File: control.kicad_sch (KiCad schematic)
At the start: 52 parts, among them J101 Cortex_Debug, J102 JAE_DX07S016JA3, J501 WAGO-2065, J502 WAGO-2065, SW101 SW_Push, SW102 SW_Push, U101 ATSAMD51G, U103 TPS78433QWDRBRQ1, Y101 32k768

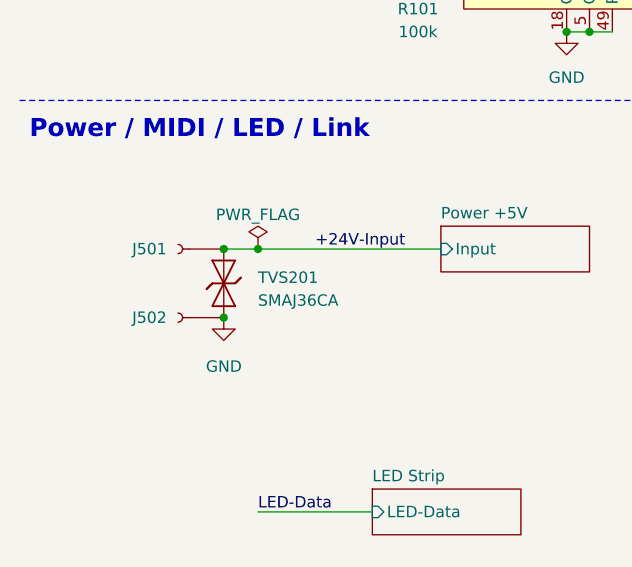
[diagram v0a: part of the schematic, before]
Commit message: Update to Kicad 8
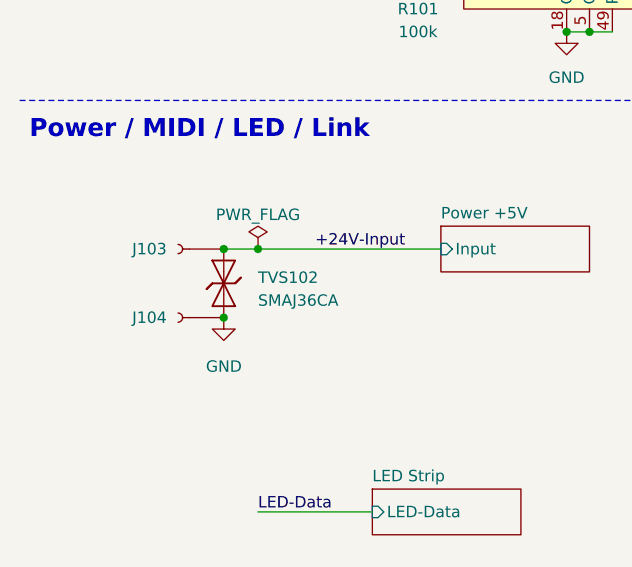
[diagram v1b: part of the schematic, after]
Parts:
- renumbered J501 to J103, J502 to J104, TVS201 to TVS102

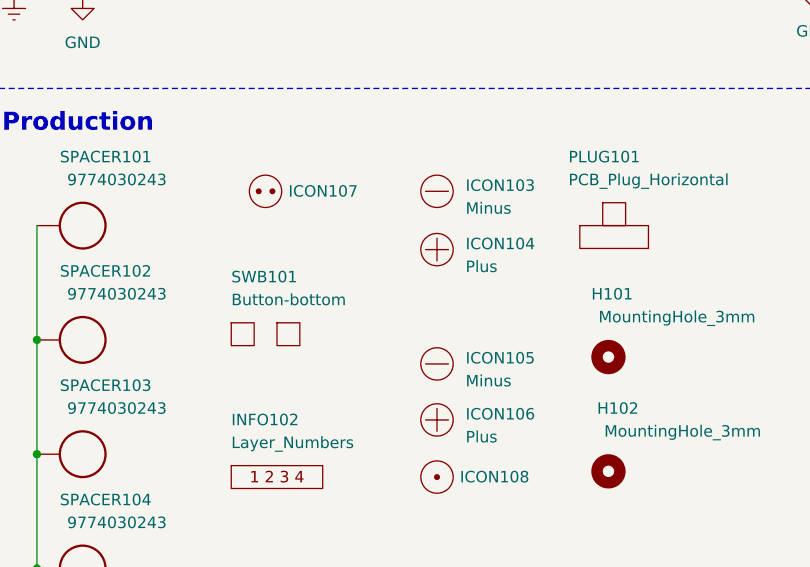
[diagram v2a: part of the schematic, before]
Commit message: Replace icons
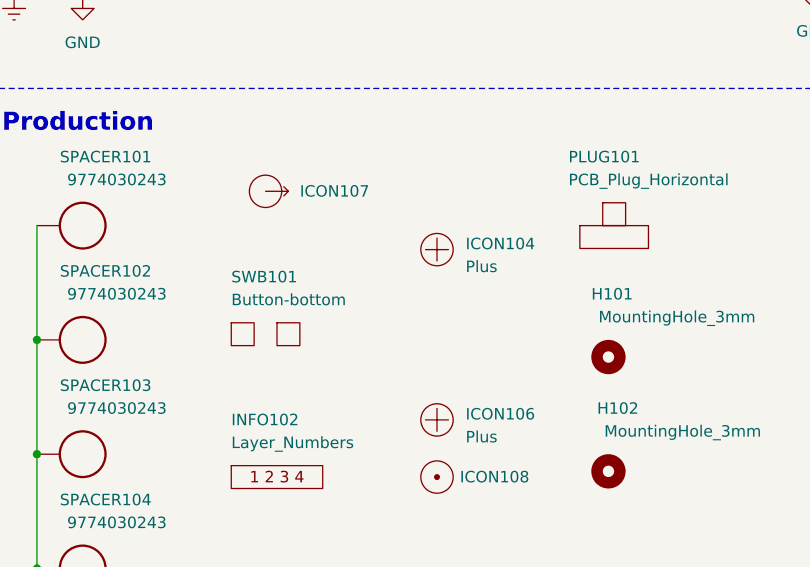
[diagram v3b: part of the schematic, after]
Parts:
- removed ICON103, ICON105: Minus, V2_Artwork:Minus_Small, symbol V2_Artwork:Minus
- removed ICON107: Socket, V2_Artwork:Socket_Small, symbol V2_Artwork:Socket
- added ICON107: Arrow_Out, V2_Artwork:Arrow_Out, symbol V2_Artwork:Arrow_Out
- U103: value TPS78433QWDRBRQ1 -> TPS78433QWDRBRQ1
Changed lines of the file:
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@@
 	)
 	(symbol
-		(lib_id "V2_Artwork:Minus")
-		(at 231.14 166.497 0)
-		(unit 1)
-		(exclude_from_sim no)
-		(in_bom no)
-		(on_board yes)
-		(dnp no)
-		(fields_autoplaced yes)
-		(property "Reference" "ICON105"
-			(at 234.315 165.862 0)
-			(effects
-				(font
-					(size 1.27 1.27)
-				)
-				(justify left)
-			)
-		)
-		(property "Value" "Minus"
-			(at 234.315 168.402 0)
-			(effects
-				(font
-					(size 1.27 1.27)
-				)
-				(justify left)
-			)
-		)
-		(property "Footprint" "V2_Artwork:Minus_Small"
-			(at 231.14 174.117 0)
-			(effects
-				(font
-					(size 1.27 1.27)
-				)
-				(hide yes)
-			)
-		)
-		(property "Datasheet" ""
-			(at 231.14 166.497 0)
-			(effects
-				(font
-					(size 1.27 1.27)
-				)
-				(hide yes)
-			)
-		)
-		(property "Description" ""
-			(at 231.14 166.497 0)
-			(effects
-				(font
-					(size 1.27 1.27)
-				)
-				(hide yes)
-			)
-		)
-		(property "Sim.Enable" "0"
-			(at 231.14 166.497 0)
-			(effects
-				(font
-					(size 1.27 1.27)
-				)
-				(hide yes)
-			)
-		)
-		(instances
-			(project "control"
-				(path "/6c8448b4-b04d-47e1-934e-e40cbe27a7be"
-					(reference "ICON105")
-					(unit 1)
-				)
-			)
-		)
-	)
-	(symbol
 		(lib_id "Device:C_Small")
 		(at 115.57 25.4 0)
@@
 	)
 	(symbol
-		(lib_id "V2_Artwork:Minus")
-		(at 231.14 147.32 0)
-		(unit 1)
-		(exclude_from_sim no)
-		(in_bom no)
-		(on_board yes)
-		(dnp no)
-		(fields_autoplaced yes)
-		(property "Reference" "ICON103"
-			(at 234.315 146.685 0)
-			(effects
-				(font
-					(size 1.27 1.27)
-				)
-				(justify left)
-			)
-		)
-		(property "Value" "Minus"
-			(at 234.315 149.225 0)
-			(effects
-				(font
-					(size 1.27 1.27)
-				)
-				(justify left)
-			)
-		)
-		(property "Footprint" "V2_Artwork:Minus_Small"
-			(at 231.14 154.94 0)
-			(effects
-				(font
-					(size 1.27 1.27)
-				)
-				(hide yes)
-			)
-		)
-		(property "Datasheet" ""
-			(at 231.14 147.32 0)
-			(effects
-				(font
-					(size 1.27 1.27)
-				)
-				(hide yes)
-			)
-		)
-		(property "Description" ""
-			(at 231.14 147.32 0)
-			(effects
-				(font
-					(size 1.27 1.27)
-				)
-				(hide yes)
-			)
-		)
-		(property "Sim.Enable" "0"
-			(at 231.14 147.32 0)
-			(effects
-				(font
-					(size 1.27 1.27)
-				)
-				(hide yes)
-			)
-		)
-		(instances
-			(project "control"
-				(path "/6c8448b4-b04d-47e1-934e-e40cbe27a7be"
-					(reference "ICON103")
-					(unit 1)
-				)
-			)
-		)
-	)
-	(symbol
 		(lib_id "V2_Production:Layer_Numbers")
 		(at 213.36 179.07 0)
 		(unit 1)
-		(exclude_from_sim no)
+		(exclude_from_sim yes)
 		(in_bom no)
 		(on_board yes)
@@
 		(at 250.19 178.435 0)
 		(unit 1)
-		(exclude_from_sim no)
+		(exclude_from_sim yes)
 		(in_bom no)
 		(on_board yes)
@@
 		(at 212.09 163.195 0)
 		(unit 1)
-		(exclude_from_sim no)
+		(exclude_from_sim yes)
 		(in_bom no)
 		(on_board yes)
@@
 		(at 250.825 151.13 0)
 		(unit 1)
-		(exclude_from_sim no)
+		(exclude_from_sim yes)
 		(in_bom no)
 		(on_board yes)
@@
 		(at 191.77 163.83 0)
 		(unit 1)
-		(exclude_from_sim no)
+		(exclude_from_sim yes)
 		(in_bom yes)
 		(on_board yes)
@@
 	)
 	(symbol
+		(lib_id "V2_Artwork:Arrow_Out")
+		(at 212.09 147.32 0)
+		(unit 1)
+		(exclude_from_sim no)
+		(in_bom no)
+		(on_board yes)
+		(dnp no)
+		(fields_autoplaced yes)
+		(property "Reference" "ICON107"
+			(at 215.9 147.3199 0)
+			(effects
+				(font
+					(size 1.27 1.27)
+				)
+				(justify left)
+			)
+		)
+		(property "Value" "Arrow_Out"
+			(at 209.55 152.4 0)
+			(effects
+				(font
+					(size 1.27 1.27)
+				)
+				(justify left bottom)
+				(hide yes)
+			)
+		)
+		(property "Footprint" "V2_Artwork:Arrow_Out"
+			(at 212.09 154.94 0)
+			(effects
+				(font
+					(size 1.27 1.27)
+				)
+				(hide yes)
+			)
+		)
+		(property "Datasheet" ""
+			(at 212.09 147.32 0)
+			(effects
+				(font
+					(size 1.27 1.27)
+				)
+				(hide yes)
+			)
+		)
+		(property "Description" ""
+			(at 212.09 147.32 0)
+			(effects
+				(font
+					(size 1.27 1.27)
+				)
+				(hide yes)
+			)
+		)
+		(property "Sim.Enable" "0"
+			(at 212.09 147.32 0)
+			(effects
+				(font
+					(size 1.27 1.27)
+				)
+				(hide yes)
+			)
+		)
+		(instances
+			(project ""
+				(path "/6c8448b4-b04d-47e1-934e-e40cbe27a7be"
+					(reference "ICON107")
+					(unit 1)
+				)
+			)
+		)
+	)
+	(symbol
 		(lib_id "power:PWR_FLAG")
 		(at 184.15 124.46 90)
@@
 		(at 127 97.79 0)
 		(unit 1)
-		(exclude_from_sim no)
+		(exclude_from_sim yes)
 		(in_bom no)
 		(on_board yes)
@@
 		(at 30.48 160.02 180)
 		(unit 1)
-		(exclude_from_sim no)
+		(exclude_from_sim yes)
 		(in_bom yes)
 		(on_board yes)
@@
 		(at 172.085 173.355 0)
 		(unit 1)
-		(exclude_from_sim no)
+		(exclude_from_sim yes)
 		(in_bom no)
 		(on_board yes)
@@
 		(at 191.77 176.53 0)
 		(unit 1)
-		(exclude_from_sim no)
+		(exclude_from_sim yes)
 		(in_bom yes)
 		(on_board yes)
@@
 	)
 	(symbol
-		(lib_id "V2_Artwork:Socket")
-		(at 212.09 147.32 0)
-		(unit 1)
-		(exclude_from_sim no)
-		(in_bom no)
-		(on_board yes)
-		(dnp no)
-		(fields_autoplaced yes)
-		(property "Reference" "ICON107"
-			(at 214.63 147.32 0)
-			(effects
-				(font
-					(size 1.27 1.27)
-				)
-				(justify left)
-			)
-		)
-		(property "Value" "Socket"
-			(at 209.55 152.4 0)
-			(effects
-				(font
-					(size 1.27 1.27)
-				)
-				(justify left bottom)
-				(hide yes)
-			)
-		)
-		(property "Footprint" "V2_Artwork:Socket_Small"
-			(at 212.09 154.94 0)
-			(effects
-				(font
-					(size 1.27 1.27)
-				)
-				(hide yes)
-			)
-		)
-		(property "Datasheet" ""
-			(at 211.9122 147.32 0)
-			(effects
-				(font
-					(size 1.27 1.27)
-				)
-				(hide yes)
-			)
-		)
-		(property "Description" ""
-			(at 212.09 147.32 0)
-			(effects
-				(font
-					(size 1.27 1.27)
-				)
-				(hide yes)
-			)
-		)
-		(property "Sim.Enable" "0"
-			(at 212.09 147.32 0)
-			(effects
-				(font
-					(size 1.27 1.27)
-				)
-				(hide yes)
-			)
-		)
-		(instances
-			(project "control"
-				(path "/6c8448b4-b04d-47e1-934e-e40cbe27a7be"
-					(reference "ICON107")
-					(unit 1)
-				)
-			)
-		)
-	)
-	(symbol
 		(lib_id "power:GND")
 		(at 247.65 27.94 270)
@@
 		(at 231.14 172.72 0)
 		(unit 1)
-		(exclude_from_sim no)
+		(exclude_from_sim yes)
 		(in_bom no)
 		(on_board yes)
@@
 		(at 172.72 186.69 0)
 		(unit 1)
-		(exclude_from_sim no)
+		(exclude_from_sim yes)
 		(in_bom no)
 		(on_board yes)
@@
 		(at 191.77 189.23 0)
 		(unit 1)
-		(exclude_from_sim no)
+		(exclude_from_sim yes)
 		(in_bom yes)
 		(on_board yes)
@@
 		(at 276.225 152.4 0)
 		(unit 1)
-		(exclude_from_sim no)
+		(exclude_from_sim yes)
 		(in_bom no)
 		(on_board yes)
@@
 		(at 250.19 165.735 0)
 		(unit 1)
-		(exclude_from_sim no)
+		(exclude_from_sim yes)
 		(in_bom no)
 		(on_board yes)
@@
 		(at 191.77 151.13 0)
 		(unit 1)
-		(exclude_from_sim no)
+		(exclude_from_sim yes)
 		(in_bom yes)
 		(on_board yes)
@@
 		(at 30.48 152.4 180)
 		(unit 1)
-		(exclude_from_sim no)
+		(exclude_from_sim yes)
 		(in_bom yes)
 		(on_board yes)
@@
 		(at 276.225 165.1 0)
 		(unit 1)
-		(exclude_from_sim no)
+		(exclude_from_sim yes)
 		(in_bom no)
 		(on_board yes)
@@
 		(at 191.77 102.87 0)
 		(unit 1)
-		(exclude_from_sim no)
+		(exclude_from_sim yes)
 		(in_bom yes)
 		(on_board yes)
@@
 		(at 231.14 179.07 0)
 		(unit 1)
-		(exclude_from_sim no)
+		(exclude_from_sim yes)
 		(in_bom no)
 		(on_board yes)
@@
 		(at 276.225 176.53 0)
 		(unit 1)
-		(exclude_from_sim no)
+		(exclude_from_sim yes)
 		(in_bom no)
 		(on_board yes)
@@
 			)
 		)
-		(property "Value" "TPS78433QWDRBRQ1 "
+		(property "Value" "TPS78433QWDRBRQ1"
 			(at 189.23 27.94 0)
 			(effects
@@
 		(at 231.14 153.797 0)
 		(unit 1)
-		(exclude_from_sim no)
+		(exclude_from_sim yes)
 		(in_bom no)
 		(on_board yes)
@@
 		(at 172.72 154.94 0)
 		(unit 1)
-		(exclude_from_sim no)
+		(exclude_from_sim yes)
 		(in_bom no)
 		(on_board yes)

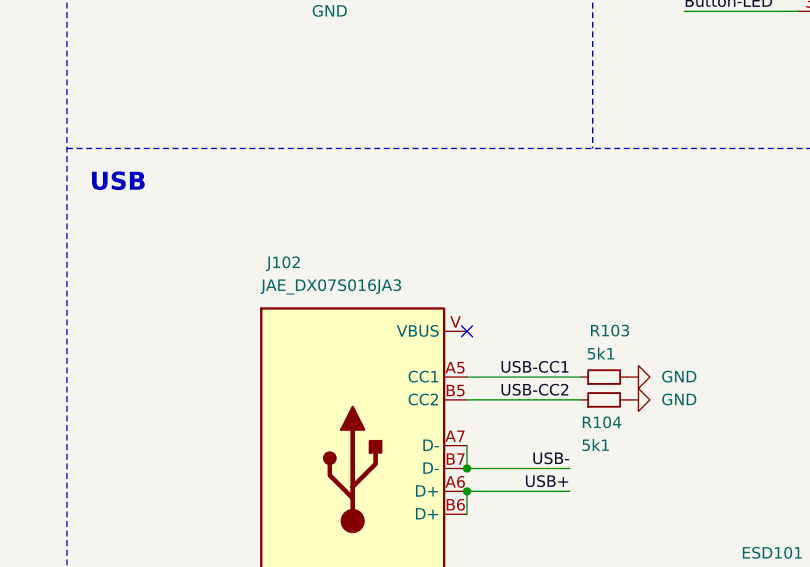
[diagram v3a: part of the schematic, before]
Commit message: Update TRS socket
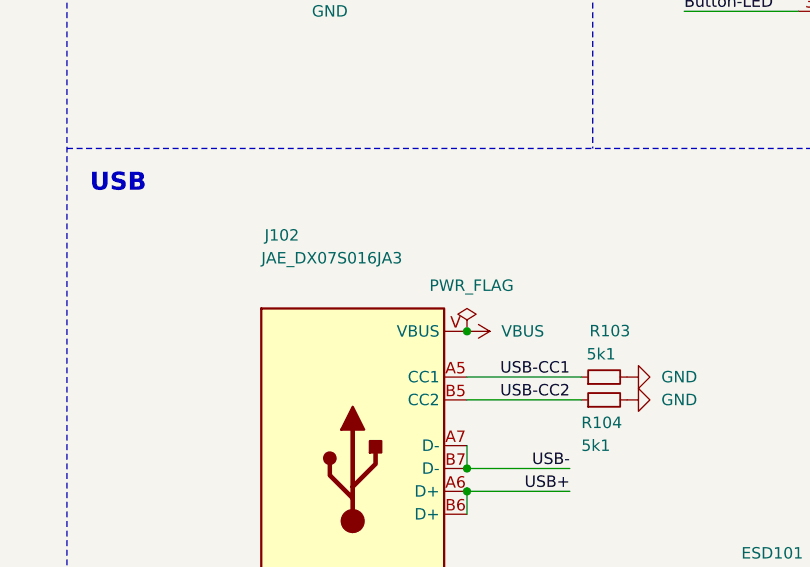
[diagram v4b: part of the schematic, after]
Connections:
- net VBUS: now reaches J102.V (VBUS)
- no-connect marks 26 -> 25
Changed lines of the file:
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@@
 	(title_block
 		(title "V2 control")
-		(date "2024-03-28")
-		(rev "4")
+		(date "2024-07-17")
+		(rev "5")
 		(company "Versio Duo")
 		(comment 1 "Instrument Controller")
@@
 	)
 	(junction
+		(at 204.47 87.63)
+		(diameter 0)
+		(color 0 0 0 0)
+	)
+	(junction
 		(at 186.69 189.23)
 		(diameter 0)
@@
 		(at 59.69 92.71)
 	)
-	(no_connect
-		(at 204.47 87.63)
-	)
 	(wire
 		(pts
@@
 		(at 213.36 179.07 0)
 		(unit 1)
-		(exclude_from_sim yes)
+		(exclude_from_sim no)
 		(in_bom no)
 		(on_board yes)
@@
 		(at 250.19 178.435 0)
 		(unit 1)
-		(exclude_from_sim yes)
+		(exclude_from_sim no)
 		(in_bom no)
 		(on_board yes)
@@
 		(at 212.09 163.195 0)
 		(unit 1)
-		(exclude_from_sim yes)
+		(exclude_from_sim no)
 		(in_bom no)
 		(on_board yes)
@@
 		(at 250.825 151.13 0)
 		(unit 1)
-		(exclude_from_sim yes)
+		(exclude_from_sim no)
 		(in_bom no)
 		(on_board yes)
@@
 		(at 191.77 163.83 0)
 		(unit 1)
-		(exclude_from_sim yes)
+		(exclude_from_sim no)
 		(in_bom yes)
 		(on_board yes)
@@
 		(at 127 97.79 0)
 		(unit 1)
-		(exclude_from_sim yes)
+		(exclude_from_sim no)
 		(in_bom no)
 		(on_board yes)
@@
 		(at 30.48 160.02 180)
 		(unit 1)
-		(exclude_from_sim yes)
+		(exclude_from_sim no)
 		(in_bom yes)
 		(on_board yes)
@@
 		(at 172.085 173.355 0)
 		(unit 1)
-		(exclude_from_sim yes)
+		(exclude_from_sim no)
 		(in_bom no)
 		(on_board yes)
@@
 		(at 191.77 176.53 0)
 		(unit 1)
-		(exclude_from_sim yes)
+		(exclude_from_sim no)
 		(in_bom yes)
 		(on_board yes)
@@
 		(at 231.14 172.72 0)
 		(unit 1)
-		(exclude_from_sim yes)
+		(exclude_from_sim no)
 		(in_bom no)
 		(on_board yes)
@@
 		(at 172.72 186.69 0)
 		(unit 1)
-		(exclude_from_sim yes)
+		(exclude_from_sim no)
 		(in_bom no)
 		(on_board yes)
@@
 		(at 191.77 189.23 0)
 		(unit 1)
-		(exclude_from_sim yes)
+		(exclude_from_sim no)
 		(in_bom yes)
 		(on_board yes)
@@
 	)
 	(symbol
+		(lib_id "power:PWR_FLAG")
+		(at 204.47 87.63 0)
+		(unit 1)
+		(exclude_from_sim no)
+		(in_bom yes)
+		(on_board yes)
+		(dnp no)
+		(property "Reference" "#FLG0104"
+			(at 204.47 85.725 0)
+			(effects
+				(font
+					(size 1.27 1.27)
+				)
+				(hide yes)
+			)
+		)
+		(property "Value" "PWR_FLAG"
+			(at 204.978 82.55 0)
+			(effects
+				(font
+					(size 1.27 1.27)
+				)
+			)
+		)
+		(property "Footprint" ""
+			(at 204.47 87.63 0)
+			(effects
+				(font
+					(size 1.27 1.27)
+				)
+				(hide yes)
+			)
+		)
+		(property "Datasheet" "~"
+			(at 204.47 87.63 0)
+			(effects
+				(font
+					(size 1.27 1.27)
+				)
+				(hide yes)
+			)
+		)
+		(property "Description" ""
+			(at 204.47 87.63 0)
+			(effects
+				(font
+					(size 1.27 1.27)
+				)
+				(hide yes)
+			)
+		)
+		(pin "1"
+		)
+		(instances
+			(project "control"
+				(path "/6c8448b4-b04d-47e1-934e-e40cbe27a7be"
+					(reference "#FLG0104")
+					(unit 1)
+				)
+			)
+		)
+	)
+	(symbol
 		(lib_id "Device:C_Small")
 		(at 175.26 39.37 0)
@@
 		(at 276.225 152.4 0)
 		(unit 1)
-		(exclude_from_sim yes)
+		(exclude_from_sim no)
 		(in_bom no)
 		(on_board yes)
@@
 	)
 	(symbol
+		(lib_id "power:VBUS")
+		(at 204.47 87.63 270)
+		(unit 1)
+		(exclude_from_sim no)
+		(in_bom yes)
+		(on_board yes)
+		(dnp no)
+		(fields_autoplaced yes)
+		(property "Reference" "#PWR0135"
+			(at 200.66 87.63 0)
+			(effects
+				(font
+					(size 1.27 1.27)
+				)
+				(hide yes)
+			)
+		)
+		(property "Value" "VBUS"
+			(at 208.28 87.6299 90)
+			(effects
+				(font
+					(size 1.27 1.27)
+				)
+				(justify left)
+			)
+		)
+		(property "Footprint" ""
+			(at 204.47 87.63 0)
+			(effects
+				(font
+					(size 1.27 1.27)
+				)
+				(hide yes)
+			)
+		)
+		(property "Datasheet" ""
+			(at 204.47 87.63 0)
+			(effects
+				(font
+					(size 1.27 1.27)
+				)
+				(hide yes)
+			)
+		)
+		(property "Description" "Power symbol creates a global label with name \"VBUS\""
+			(at 204.47 87.63 0)
+			(effects
+				(font
+					(size 1.27 1.27)
+				)
+				(hide yes)
+			)
+		)
+		(pin "1"
+		)
+		(instances
+			(project "control"
+				(path "/6c8448b4-b04d-47e1-934e-e40cbe27a7be"
+					(reference "#PWR0135")
+					(unit 1)
+				)
+			)
+		)
+	)
+	(symbol
 		(lib_id "power:Earth")
 		(at 184.15 125.73 0)
@@
 		(at 250.19 165.735 0)
 		(unit 1)
-		(exclude_from_sim yes)
+		(exclude_from_sim no)
 		(in_bom no)
 		(on_board yes)
@@
 		(at 191.77 151.13 0)
 		(unit 1)
-		(exclude_from_sim yes)
+		(exclude_from_sim no)
 		(in_bom yes)
 		(on_board yes)
@@
 		(at 30.48 152.4 180)
 		(unit 1)
-		(exclude_from_sim yes)
+		(exclude_from_sim no)
 		(in_bom yes)
 		(on_board yes)
@@
 		(at 276.225 165.1 0)
 		(unit 1)
-		(exclude_from_sim yes)
+		(exclude_from_sim no)
 		(in_bom no)
 		(on_board yes)
@@
 		(at 191.77 102.87 0)
 		(unit 1)
-		(exclude_from_sim yes)
+		(exclude_from_sim no)
 		(in_bom yes)
 		(on_board yes)
 		(dnp no)
 		(property "Reference" "J102"
-			(at 184.15 80.01 0)
+			(at 183.896 76.962 0)
 			(effects
 				(font
@@
 		)
 		(property "Value" "JAE_DX07S016JA3"
-			(at 181.61 82.55 0)
+			(at 181.61 79.502 0)
 			(effects
 				(font
@@
 		(at 231.14 179.07 0)
 		(unit 1)
-		(exclude_from_sim yes)
+		(exclude_from_sim no)
 		(in_bom no)
 		(on_board yes)
@@
 		(at 276.225 176.53 0)
 		(unit 1)
-		(exclude_from_sim yes)
+		(exclude_from_sim no)
 		(in_bom no)
 		(on_board yes)
@@
 		(at 231.14 153.797 0)
 		(unit 1)
-		(exclude_from_sim yes)
+		(exclude_from_sim no)
 		(in_bom no)
 		(on_board yes)
@@
 		(at 172.72 154.94 0)
 		(unit 1)
-		(exclude_from_sim yes)
+		(exclude_from_sim no)
 		(in_bom no)
 		(on_board yes)

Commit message: Refresh
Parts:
- removed C104: 0u1, Capacitor_SMD:C_0603_1608Metric, symbol Device:C_Small
- renumbered C103 to C101, C105 to C102, C106 to C103, C107 to C104, C108 to C105, C110 to C106, C109 to C107, C101 to C108, C102 to C109, C111 to C110, D102 to D101, D103 to D102, D101 to D103, ICON107 to ICON101, ICON104 to ICON102, ICON102 to ICON103, ICON106 to ICON104, ICON101 to ICON105, ICON108 to ICON106, INFO102 to INFO101, INFO101 to INFO102, R102 to R101, R105 to R102, R101 to R105, SW102 to SW101, SW101 to SW102, U103 to U101, U101 to U102
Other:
- moved on the sheet: C101
